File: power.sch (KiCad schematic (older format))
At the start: 24 parts, among them U10 LM1117-3.3, U16 R-78E5.0-1.0, U3 STMPS2151, U7 LM1117-3.3

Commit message: added package field
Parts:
- C1, C15, C2, C20, C32, C36, C9, L1, L2, R5, R6: Package (none) -> 0603
- C14, C47: Package (none) -> Panasonic D
- C25, C41, C5: Package (none) -> Panasonic C
- D1: Package (none) -> SOT-23
- D3, D4: Package (none) -> SOD-123
- U10, U7: Package (none) -> SOT-223
- U3: Package (none) -> SOT-23-5
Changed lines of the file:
@@
 F 4 "Diodes Inc." H 1650 2800 50  0001 C CNN "MFN"
 F 5 "1N5819HW-7-F" H 1650 2800 50  0001 C CNN "MFP"
+F 6 "SOD-123" H 1650 2800 50  0001 C CNN "Package"
 	1    1650 2600
 	1    0    0    -1
@@
 F 4 "Diodes Inc." H 1650 3200 50  0001 C CNN "MFN"
 F 5 "1N5819HW-7-F" H 1650 3200 50  0001 C CNN "MFP"
+F 6 "SOD-123" H 1650 3200 50  0001 C CNN "Package"
 	1    1650 3000
 	-1   0    0    1
@@
 F 4 "Panasonic" H 3800 2550 60  0001 C CNN "MFN"
 F 5 "EEE-FK1V470P" H 3800 2550 60  0001 C CNN "MFP"
+F 6 "Panasonic D" H 3825 2750 50  0001 C CNN "Package"
 	1    3800 2550
 	1    0    0    -1
@@
 F 4 "Texas Instruments" H 5500 3700 60  0001 C CNN "MFN"
 F 5 "LM1117MP-3.3/NOPB" H 5500 3700 60  0001 C CNN "MFP"
+F 6 "SOT-223" H 5350 3925 50  0001 C CNN "Package"
 	1    5500 3700
 	1    0    0    -1
@@
 F 4 "Laird" H 4750 3700 60  0001 C CNN "MFN"
 F 5 "MI0603K300R-10" H 4750 3700 60  0001 C CNN "MFP"
+F 6 "0603" H 4600 3825 50  0001 C CNN "Package"
 	1    4750 3700
 	0    1    1    0
@@
 F 4 "Panasonic" H 6000 3950 60  0001 C CNN "MFN"
 F 5 "EEE-FP1E220AR" H 6000 3950 60  0001 C CNN "MFP"
+F 6 "Panasonic C" H 6025 4150 50  0001 C CNN "Package"
 	1    6000 3950
 	1    0    0    -1
@@
 F 4 "Murata" H 6325 4150 50  0001 C CNN "MFN"
 F 5 "GRM188R71E104JA01J" H 6325 4150 50  0001 C CNN "MFP"
+F 6 "0603" H 6325 4150 50  0001 C CNN "Package"
 	1    6300 3950
 	1    0    0    -1
@@
 F 4 "Texas Instruments" H 5500 4800 60  0001 C CNN "MFN"
 F 5 "LM1117MP-3.3/NOPB" H 5500 4800 60  0001 C CNN "MFP"
+F 6 "SOT-223" H 5350 5025 50  0001 C CNN "Package"
 	1    5500 4800
 	1    0    0    -1
@@
 F 4 "Murata" H 6325 5250 50  0001 C CNN "MFN"
 F 5 "GRM188R71E104JA01J" H 6325 5250 50  0001 C CNN "MFP"
+F 6 "0603" H 6325 5250 50  0001 C CNN "Package"
 	1    6300 5050
 	1    0    0    -1
@@
 F 4 "Murata" H 6225 2850 50  0001 C CNN "MFN"
 F 5 "GRM188R71E104JA01J" H 6225 2850 50  0001 C CNN "MFP"
+F 6 "0603" H 6225 2850 50  0001 C CNN "Package"
 	1    6200 2650
 	1    0    0    -1
@@
 F 4 "Texas Instruments" H 7900 3050 60  0001 C CNN "MFN"
 F 5 "LM4040CIM3-10.0/NOPB" H 7900 3050 60  0001 C CNN "MFP"
+F 6 "SOT-23" H 7900 3250 50  0001 C CNN "Package"
 	1    7900 3050
 	0    -1   -1   0
@@
 F 4 "Panasonic" H 7980 2650 50  0001 C CNN "MFN"
 F 5 "ERJ-3EKF1001V" H 7980 2650 50  0001 C CNN "MFP"
+F 6 "0603" H 7980 2650 50  0001 C CNN "Package"
 	1    7900 2550
 	1    0    0    -1
@@
 F 4 "Murata" H 8225 3250 50  0001 C CNN "MFN"
 F 5 "GRM188R71E104JA01J" H 8225 3250 50  0001 C CNN "MFP"
+F 6 "0603" H 8225 3250 50  0001 C CNN "Package"
 	1    8200 3050
 	1    0    0    -1
@@
 F 4 "STMicroelectronics" H 8900 4200 60  0001 C CNN "MFN"
 F 5 "STMPS2151STR" H 8900 4200 60  0001 C CNN "MFP"
+F 6 "SOT-23-5" H 8900 4500 50  0001 C CNN "Package"
 	1    8900 4200
 	1    0    0    -1
@@
 F 4 "Panasonic" H 8280 4550 50  0001 C CNN "MFN"
 F 5 "ERJ-3EKF1002V" H 8280 4550 50  0001 C CNN "MFP"
+F 6 "0603" H 8280 4550 50  0001 C CNN "Package"
 	1    8200 4450
 	1    0    0    -1
@@
 F 4 "Panasonic" H 3800 3050 60  0001 C CNN "MFN"
 F 5 "EEE-FK1V470P" H 3800 3050 60  0001 C CNN "MFP"
+F 6 "Panasonic D" H 3825 3250 50  0001 C CNN "Package"
 	1    3800 3050
 	1    0    0    -1
@@
 F 4 "Panasonic" H 6000 5050 60  0001 C CNN "MFN"
 F 5 "EEE-FP1E220AR" H 6000 5050 60  0001 C CNN "MFP"
+F 6 "Panasonic C" H 6025 5250 50  0001 C CNN "Package"
 	1    6000 5050
 	1    0    0    -1
@@
 F 4 "Panasonic" H 5900 2650 60  0001 C CNN "MFN"
 F 5 "EEE-FP1E220AR" H 5900 2650 60  0001 C CNN "MFP"
+F 6 "Panasonic C" H 5925 2850 50  0001 C CNN "Package"
 	1    5900 2650
 	1    0    0    -1
@@
 F 4 "Laird" H 4750 4800 60  0001 C CNN "MFN"
 F 5 "MI0603K300R-10" H 4750 4800 60  0001 C CNN "MFP"
+F 6 "0603" H 4600 4925 50  0001 C CNN "Package"
 	1    4750 4800
 	0    1    1    0
@@
 F 4 "Murata" H 5000 3950 60  0001 C CNN "MFN"
 F 5 "GRM188R71E104JA01J" H 5000 3950 60  0001 C CNN "MFP"
+F 6 "0603" H 5025 4150 50  0001 C CNN "Package"
 	1    5000 3950
 	1    0    0    -1
@@
 F 4 "Murata" H 5000 5050 60  0001 C CNN "MFN"
 F 5 "GRM188R71E104JA01J" H 5000 5050 60  0001 C CNN "MFP"
+F 6 "0603" H 5025 5250 50  0001 C CNN "Package"
 	1    5000 5050
 	1    0    0    -1
@@
 F 4 "Murata" H 4800 2650 60  0001 C CNN "MFN"
 F 5 "GRM188R71E104JA01J" H 4800 2650 60  0001 C CNN "MFP"
+F 6 "0603" H 4825 2850 50  0001 C CNN "Package"
 	1    4800 2650
 	1    0    0    -1

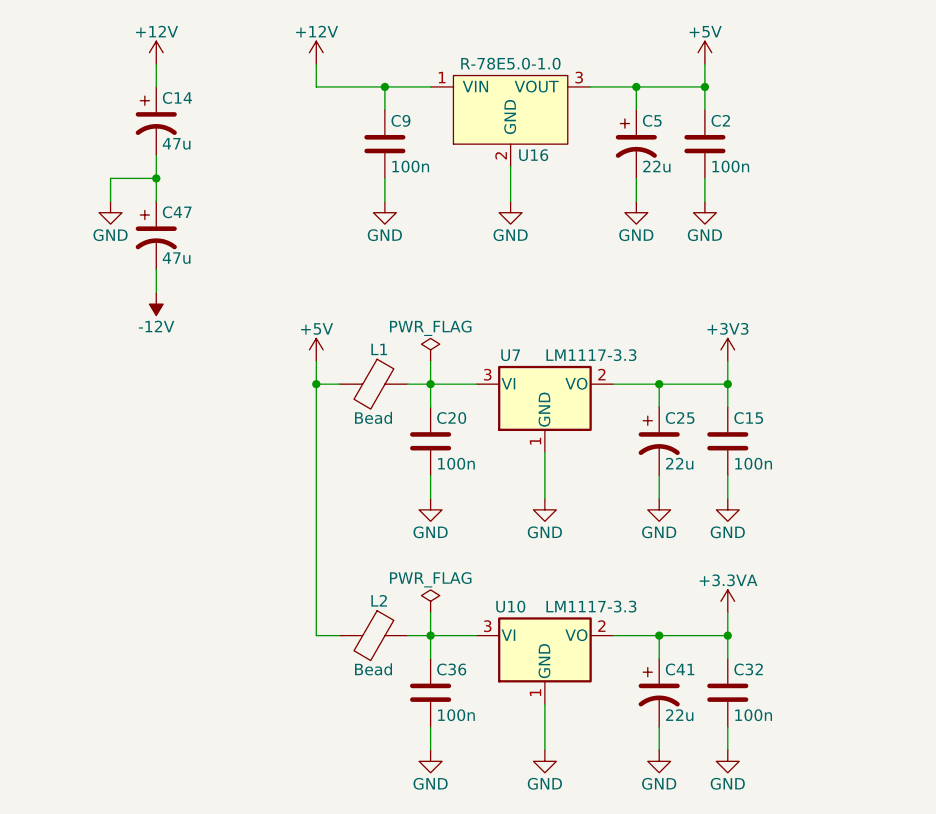
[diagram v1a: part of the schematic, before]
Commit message: renumbered components
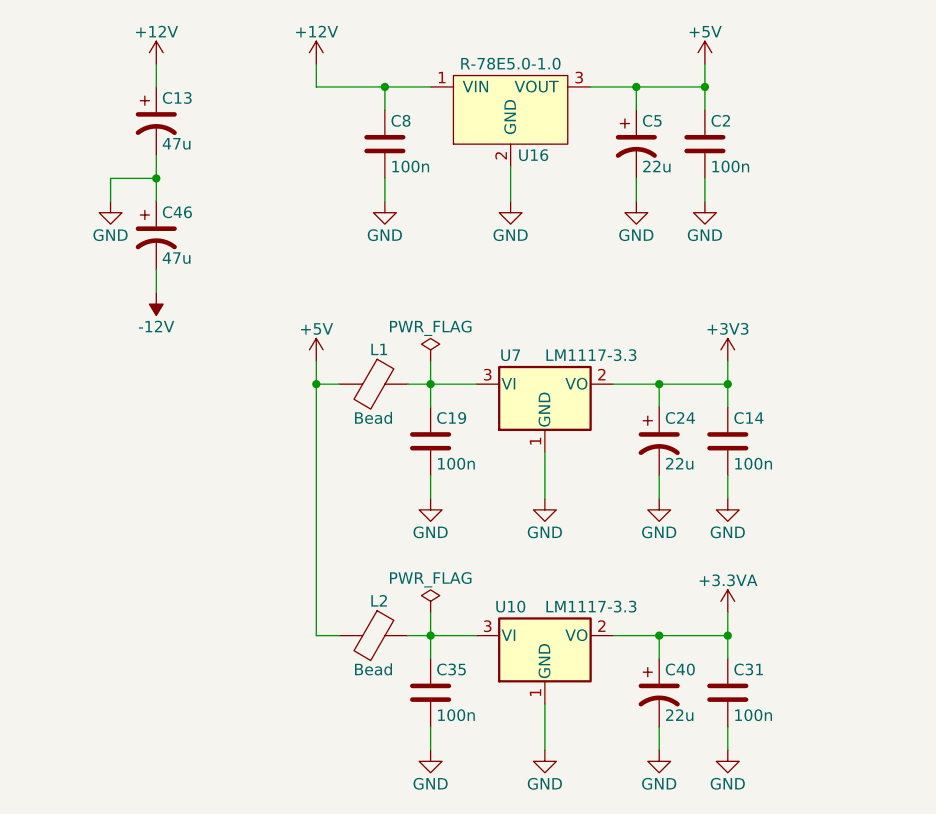
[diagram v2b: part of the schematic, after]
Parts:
- renumbered C14 to C13, C15 to C14, C20 to C19, C25 to C24, C32 to C31, C36 to C35, C41 to C40, C47 to C46, C9 to C8
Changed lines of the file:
@@
 $EndComp
 $Comp
-L CP1 C14
+L CP1 C13
 U 1 1 59ADD50C
 P 3800 2550
-F 0 "C14" H 3825 2650 50  0000 L CNN
+F 0 "C13" H 3825 2650 50  0000 L CNN
 F 1 "47u" H 3825 2450 50  0000 L CNN
 F 2 "Capacitors_SMD:CP_Elec_6.3x5.7" H 3800 2550 50  0001 C CNN
@@
 $EndComp
 $Comp
-L CP1 C25
+L CP1 C24
 U 1 1 59DEC56E
 P 6000 3950
-F 0 "C25" H 6025 4050 50  0000 L CNN
+F 0 "C24" H 6025 4050 50  0000 L CNN
 F 1 "22u" H 6025 3850 50  0000 L CNN
 F 2 "Capacitors_SMD:CP_Elec_5x5.8" H 6000 3950 50  0001 C CNN
@@
 $EndComp
 $Comp
-L C C15
+L C C14
 U 1 1 59DEC574
 P 6300 3950
-F 0 "C15" H 6325 4050 50  0000 L CNN
+F 0 "C14" H 6325 4050 50  0000 L CNN
 F 1 "100n" H 6325 3850 50  0000 L CNN
 F 2 "w_capacitor:C_0603" H 6338 3800 50  0001 C CNN
@@
 $EndComp
 $Comp
-L C C32
+L C C31
 U 1 1 59DEC80C
 P 6300 5050
-F 0 "C32" H 6325 5150 50  0000 L CNN
+F 0 "C31" H 6325 5150 50  0000 L CNN
 F 1 "100n" H 6325 4950 50  0000 L CNN
 F 2 "w_capacitor:C_0603" H 6338 4900 50  0001 C CNN
@@
 $EndComp
 $Comp
-L CP1 C47
+L CP1 C46
 U 1 1 59E0E120
 P 3800 3050
-F 0 "C47" H 3825 3150 50  0000 L CNN
+F 0 "C46" H 3825 3150 50  0000 L CNN
 F 1 "47u" H 3825 2950 50  0000 L CNN
 F 2 "Capacitors_SMD:CP_Elec_6.3x5.7" H 3800 3050 50  0001 C CNN
@@
 $EndComp
 $Comp
-L CP1 C41
+L CP1 C40
 U 1 1 59E0FE4F
 P 6000 5050
-F 0 "C41" H 6025 5150 50  0000 L CNN
+F 0 "C40" H 6025 5150 50  0000 L CNN
 F 1 "22u" H 6025 4950 50  0000 L CNN
 F 2 "Capacitors_SMD:CP_Elec_5x5.8" H 6000 5050 50  0001 C CNN
@@
 $EndComp
 $Comp
-L C C20
+L C C19
 U 1 1 59E52EDD
 P 5000 3950
-F 0 "C20" H 5025 4050 50  0000 L CNN
+F 0 "C19" H 5025 4050 50  0000 L CNN
 F 1 "100n" H 5025 3850 50  0000 L CNN
 F 2 "w_capacitor:C_0603" H 5038 3800 50  0001 C CNN
@@
 $EndComp
 $Comp
-L C C36
+L C C35
 U 1 1 59E53513
 P 5000 5050
-F 0 "C36" H 5025 5150 50  0000 L CNN
+F 0 "C35" H 5025 5150 50  0000 L CNN
 F 1 "100n" H 5025 4950 50  0000 L CNN
 F 2 "w_capacitor:C_0603" H 5038 4900 50  0001 C CNN
@@
 $EndComp
 $Comp
-L C C9
+L C C8
 U 1 1 59E535E8
 P 4800 2650
-F 0 "C9" H 4825 2750 50  0000 L CNN
+F 0 "C8" H 4825 2750 50  0000 L CNN
 F 1 "100n" H 4825 2550 50  0000 L CNN
 F 2 "w_capacitor:C_0603" H 4838 2500 50  0001 C CNN

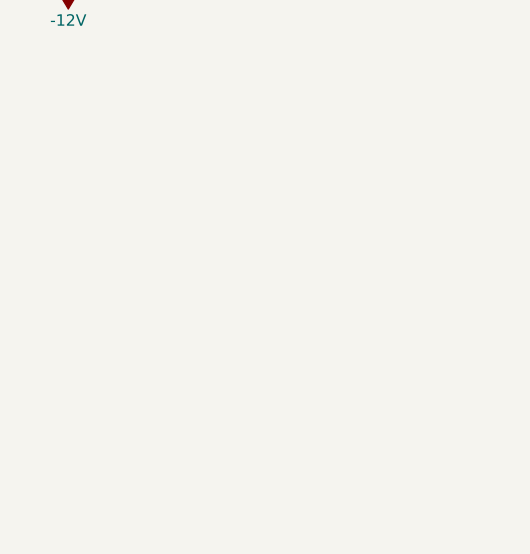
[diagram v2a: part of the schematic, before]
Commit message: cleanup schematics and updated to revision 0.3
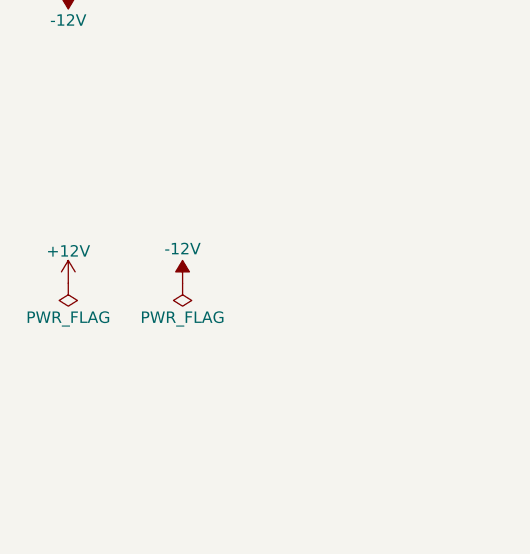
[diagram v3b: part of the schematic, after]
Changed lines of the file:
@@
 Sheet 3 8
 Title "per|former eurorack sequencer"
-Date ""
-Rev "0.2"
+Date "2018-08-26"
+Rev "0.3"
 Comp "westlicht"
 Comment1 "cc-by-sa"
@@
 $EndDescr
 $Comp
-L +12V #PWR025
+L +12V #PWR5
 U 1 1 59ADCE23
 P 1400 2500
-F 0 "#PWR025" H 1400 2350 50  0001 C CNN
+F 0 "#PWR5" H 1400 2350 50  0001 C CNN
 F 1 "+12V" H 1400 2640 50  0000 C CNN
 F 2 "" H 1400 2500 50  0001 C CNN
@@
 $EndComp
 $Comp
-L -12V #PWR212
+L -12V #PWR12
 U 1 1 59ADCE37
 P 1400 3100
-F 0 "#PWR212" H 1400 3200 50  0001 C CNN
+F 0 "#PWR12" H 1400 3200 50  0001 C CNN
 F 1 "-12V" H 1400 3250 50  0000 C CNN
 F 2 "" H 1400 3100 50  0001 C CNN
@@
 $EndComp
 $Comp
-L GND #PWR026
+L GND #PWR6
 U 1 1 59ADD2AE
 P 2800 2900
-F 0 "#PWR026" H 2800 2650 50  0001 C CNN
+F 0 "#PWR6" H 2800 2650 50  0001 C CNN
 F 1 "GND" H 2800 2750 50  0000 C CNN
 F 2 "" H 2800 2900 50  0001 C CNN
@@
 $EndComp
 $Comp
-L -12V #PWR213
+L -12V #PWR13
 U 1 1 59ADD571
 P 3800 3300
-F 0 "#PWR213" H 3800 3400 50  0001 C CNN
+F 0 "#PWR13" H 3800 3400 50  0001 C CNN
 F 1 "-12V" H 3800 3450 50  0000 C CNN
 F 2 "" H 3800 3300 50  0001 C CNN
@@
 $EndComp
 $Comp
-L +12V #PWR027
+L +12V #PWR1
 U 1 1 59ADD597
 P 3800 2300
-F 0 "#PWR027" H 3800 2150 50  0001 C CNN
+F 0 "#PWR1" H 3800 2150 50  0001 C CNN
 F 1 "+12V" H 3800 2440 50  0000 C CNN
 F 2 "" H 3800 2300 50  0001 C CNN
@@
 $EndComp
 $Comp
-L GND #PWR028
+L GND #PWR7
 U 1 1 59ADD670
 P 3600 2900
-F 0 "#PWR028" H 3600 2650 50  0001 C CNN
+F 0 "#PWR7" H 3600 2650 50  0001 C CNN
 F 1 "GND" H 3600 2750 50  0000 C CNN
 F 2 "" H 3600 2900 50  0001 C CNN
@@
 $EndComp
 $Comp
-L GND #PWR029
+L GND #PWR18
 U 1 1 59DEC57A
 P 5000 4200
-F 0 "#PWR029" H 5000 3950 50  0001 C CNN
+F 0 "#PWR18" H 5000 3950 50  0001 C CNN
 F 1 "GND" H 5000 4050 50  0000 C CNN
 F 2 "" H 5000 4200 50  0001 C CNN
@@
 $EndComp
 $Comp
-L GND #PWR030
+L GND #PWR20
 U 1 1 59DEC580
 P 6000 4200
-F 0 "#PWR030" H 6000 3950 50  0001 C CNN
+F 0 "#PWR20" H 6000 3950 50  0001 C CNN
 F 1 "GND" H 6000 4050 50  0000 C CNN
 F 2 "" H 6000 4200 50  0001 C CNN
@@
 $EndComp
 $Comp
-L GND #PWR031
+L GND #PWR21
 U 1 1 59DEC586
 P 6300 4200
-F 0 "#PWR031" H 6300 3950 50  0001 C CNN
+F 0 "#PWR21" H 6300 3950 50  0001 C CNN
 F 1 "GND" H 6300 4050 50  0000 C CNN
 F 2 "" H 6300 4200 50  0001 C CNN
@@
 $EndComp
 $Comp
-L +3V3 #PWR032
+L +3V3 #PWR16
 U 1 1 59DEC592
 P 6300 3600
-F 0 "#PWR032" H 6300 3450 50  0001 C CNN
+F 0 "#PWR16" H 6300 3450 50  0001 C CNN
 F 1 "+3V3" H 6300 3740 50  0000 C CNN
 F 2 "" H 6300 3600 50  0001 C CNN
@@
 $EndComp
 $Comp
-L GND #PWR033
+L GND #PWR19
 U 1 1 59DEC598
 P 5500 4200
-F 0 "#PWR033" H 5500 3950 50  0001 C CNN
+F 0 "#PWR19" H 5500 3950 50  0001 C CNN
 F 1 "GND" H 5500 4050 50  0000 C CNN
 F 2 "" H 5500 4200 50  0001 C CNN
@@
 $EndComp
 $Comp
-L GND #PWR034
+L GND #PWR27
 U 1 1 59DEC812
 P 5000 5300
-F 0 "#PWR034" H 5000 5050 50  0001 C CNN
+F 0 "#PWR27" H 5000 5050 50  0001 C CNN
 F 1 "GND" H 5000 5150 50  0000 C CNN
 F 2 "" H 5000 5300 50  0001 C CNN
@@
 $EndComp
 $Comp
-L GND #PWR035
+L GND #PWR29
 U 1 1 59DEC818
 P 6000 5300
-F 0 "#PWR035" H 6000 5050 50  0001 C CNN
+F 0 "#PWR29" H 6000 5050 50  0001 C CNN
 F 1 "GND" H 6000 5150 50  0000 C CNN
 F 2 "" H 6000 5300 50  0001 C CNN
@@
 $EndComp
 $Comp
-L GND #PWR036
+L GND #PWR30
 U 1 1 59DEC81E
 P 6300 5300
-F 0 "#PWR036" H 6300 5050 50  0001 C CNN
+F 0 "#PWR30" H 6300 5050 50  0001 C CNN
 F 1 "GND" H 6300 5150 50  0000 C CNN
 F 2 "" H 6300 5300 50  0001 C CNN
@@
 $EndComp
 $Comp
-L GND #PWR037
+L GND #PWR28
 U 1 1 59DEC82A
 P 5500 5300
-F 0 "#PWR037" H 5500 5050 50  0001 C CNN
+F 0 "#PWR28" H 5500 5050 50  0001 C CNN
 F 1 "GND" H 5500 5150 50  0000 C CNN
 F 2 "" H 5500 5300 50  0001 C CNN
@@
 $EndComp
 $Comp
-L +12V #PWR038
+L +12V #PWR2
 U 1 1 59DECCAB
 P 4500 2300
-F 0 "#PWR038" H 4500 2150 50  0001 C CNN
+F 0 "#PWR2" H 4500 2150 50  0001 C CNN
 F 1 "+12V" H 4500 2440 50  0000 C CNN
 F 2 "" H 4500 2300 50  0001 C CNN
@@
 $EndComp
 $Comp
-L +3.3VA #PWR039
+L +3.3VA #PWR24
 U 1 1 59DED3E1
 P 6300 4700
-F 0 "#PWR039" H 6300 4550 50  0001 C CNN
+F 0 "#PWR24" H 6300 4550 50  0001 C CNN
 F 1 "+3.3VA" H 6300 4840 50  0000 C CNN
 F 2 "" H 6300 4700 50  0001 C CNN
@@
 $EndComp
 $Comp
-L GND #PWR040
+L GND #PWR8
 U 1 1 59DED9CB
 P 4800 2900
-F 0 "#PWR040" H 4800 2650 50  0001 C CNN
+F 0 "#PWR8" H 4800 2650 50  0001 C CNN
 F 1 "GND" H 4800 2750 50  0000 C CNN
 F 2 "" H 4800 2900 50  0001 C CNN
@@
 $EndComp
 $Comp
-L GND #PWR041
+L GND #PWR10
 U 1 1 59DED9D1
 P 5900 2900
-F 0 "#PWR041" H 5900 2650 50  0001 C CNN
+F 0 "#PWR10" H 5900 2650 50  0001 C CNN
 F 1 "GND" H 5900 2750 50  0000 C CNN
 F 2 "" H 5900 2900 50  0001 C CNN
@@
 $EndComp
 $Comp
-L GND #PWR042
+L GND #PWR11
 U 1 1 59DED9D7
 P 6200 2900
-F 0 "#PWR042" H 6200 2650 50  0001 C CNN
+F 0 "#PWR11" H 6200 2650 50  0001 C CNN
 F 1 "GND" H 6200 2750 50  0000 C CNN
 F 2 "" H 6200 2900 50  0001 C CNN
@@
 $EndComp
 $Comp
-L GND #PWR043
+L GND #PWR9
 U 1 1 59DED9DD
 P 5350 2900
-F 0 "#PWR043" H 5350 2650 50  0001 C CNN
+F 0 "#PWR9" H 5350 2650 50  0001 C CNN
 F 1 "GND" H 5350 2750 50  0000 C CNN
 F 2 "" H 5350 2900 50  0001 C CNN
@@
 $EndComp
 $Comp
-L +5V #PWR044
+L +5V #PWR3
 U 1 1 59DEDB3A
 P 6200 2300
-F 0 "#PWR044" H 6200 2150 50  0001 C CNN
+F 0 "#PWR3" H 6200 2150 50  0001 C CNN
 F 1 "+5V" H 6200 2440 50  0000 C CNN
 F 2 "" H 6200 2300 50  0001 C CNN
@@
 $EndComp
 $Comp
-L -12V #PWR204
+L -12V #PWR4
 U 1 1 59DF1046
 P 7900 2300
-F 0 "#PWR204" H 7900 2400 50  0001 C CNN
+F 0 "#PWR4" H 7900 2400 50  0001 C CNN
 F 1 "-12V" H 7900 2450 50  0000 C CNN
 F 2 "" H 7900 2300 50  0001 C CNN
@@
 $EndComp
 $Comp
-L GND #PWR045
+L GND #PWR14
 U 1 1 59DF1FC9
 P 7900 3400
-F 0 "#PWR045" H 7900 3150 50  0001 C CNN
+F 0 "#PWR14" H 7900 3150 50  0001 C CNN
 F 1 "GND" H 7900 3250 50  0000 C CNN
 F 2 "" H 7900 3400 50  0001 C CNN
@@
 $EndComp
 $Comp
-L +5V #PWR046
+L +5V #PWR17
 U 1 1 59DFDC6E
 P 8400 4000
-F 0 "#PWR046" H 8400 3850 50  0001 C CNN
+F 0 "#PWR17" H 8400 3850 50  0001 C CNN
 F 1 "+5V" H 8400 4140 50  0000 C CNN
 F 2 "" H 8400 4000 50  0001 C CNN
@@
 $EndComp
 $Comp
-L GND #PWR047
+L GND #PWR26
 U 1 1 59DFDCE5
 P 8400 4700
-F 0 "#PWR047" H 8400 4450 50  0001 C CNN
+F 0 "#PWR26" H 8400 4450 50  0001 C CNN
 F 1 "GND" H 8400 4550 50  0000 C CNN
 F 2 "" H 8400 4700 50  0001 C CNN
@@
 $EndComp
 $Comp
-L GND #PWR048
+L GND #PWR25
 U 1 1 59E00E5E
 P 8200 4700
-F 0 "#PWR048" H 8200 4450 50  0001 C CNN
+F 0 "#PWR25" H 8200 4450 50  0001 C CNN
 F 1 "GND" H 8200 4550 50  0000 C CNN
 F 2 "" H 8200 4700 50  0001 C CNN
@@
 $EndComp
 $Comp
-L PWR_FLAG #FLG049
+L PWR_FLAG #FLG1
 U 1 1 59F34CFD
 P 5000 3600
-F 0 "#FLG049" H 5000 3675 50  0001 C CNN
+F 0 "#FLG1" H 5000 3675 50  0001 C CNN
 F 1 "PWR_FLAG" H 5000 3750 50  0000 C CNN
 F 2 "" H 5000 3600 50  0001 C CNN
@@
 $EndComp
 $Comp
-L PWR_FLAG #FLG050
+L PWR_FLAG #FLG4
 U 1 1 59F34D75
 P 5000 4700
-F 0 "#FLG050" H 5000 4775 50  0001 C CNN
+F 0 "#FLG4" H 5000 4775 50  0001 C CNN
 F 1 "PWR_FLAG" H 5000 4850 50  0000 C CNN
 F 2 "" H 5000 4700 50  0001 C CNN
@@
 $EndComp
 $Comp
-L +5V #PWR051
+L +5V #PWR15
 U 1 1 5AEF8A3B
 P 4500 3600
-F 0 "#PWR051" H 4500 3450 50  0001 C CNN
+F 0 "#PWR15" H 4500 3450 50  0001 C CNN
 F 1 "+5V" H 4500 3740 50  0000 C CNN
 F 2 "" H 4500 3600 50  0001 C CNN
@@
 Connection ~ 8200 4200
 Connection ~ 7900 2800
+$Comp
+L +12V #PWR22
+U 1 1 5B8366B1
+P 1400 4400
+F 0 "#PWR22" H 1400 4250 50  0001 C CNN
+F 1 "+12V" H 1400 4540 50  0000 C CNN
+F 2 "" H 1400 4400 50  0001 C CNN
+F 3 "" H 1400 4400 50  0001 C CNN
+	1    1400 4400
+	1    0    0    -1
+$EndComp
+$Comp
+L -12V #PWR23
+U 1 1 5B83670D
+P 1900 4400
+F 0 "#PWR23" H 1900 4500 50  0001 C CNN
+F 1 "-12V" H 1900 4550 50  0000 C CNN
+F 2 "" H 1900 4400 50  0001 C CNN
+F 3 "" H 1900 4400 50  0001 C CNN
+	1    1900 4400
+	1    0    0    -1
+$EndComp
+$Comp
+L PWR_FLAG #FLG2
+U 1 1 5B836769
+P 1400 4400
+F 0 "#FLG2" H 1400 4475 50  0001 C CNN
+F 1 "PWR_FLAG" H 1400 4550 50  0000 C CNN
+F 2 "" H 1400 4400 50  0001 C CNN
+F 3 "" H 1400 4400 50  0001 C CNN
+	1    1400 4400
+	-1   0    0    1
+$EndComp
+$Comp
+L PWR_FLAG #FLG3
+U 1 1 5B836855
+P 1900 4400
+F 0 "#FLG3" H 1900 4475 50  0001 C CNN
+F 1 "PWR_FLAG" H 1900 4550 50  0000 C CNN
+F 2 "" H 1900 4400 50  0001 C CNN
+F 3 "" H 1900 4400 50  0001 C CNN
+	1    1900 4400
+	-1   0    0    1
+$EndComp
 $EndSCHEMATC

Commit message: cleaned up schematics
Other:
- note added: "-10V REFERENCE"
- note added: "3.3V SUPPLY (ANALOG)"
- note added: "3.3V SUPPLY (DIGITAL)"
- note added: "5V 1A DC-DC step down converter"
- note added: "5V SUPPLY"
- note added: "5V SUPPLY (USB)"
- note added: "POWER INLET"
- note added: "Reverse protection and filtering for +12V/-12V rails"
- moved on the sheet: C1, C13, C14, C19, C2, C24, C31, C35, C40, C46, C5, C8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

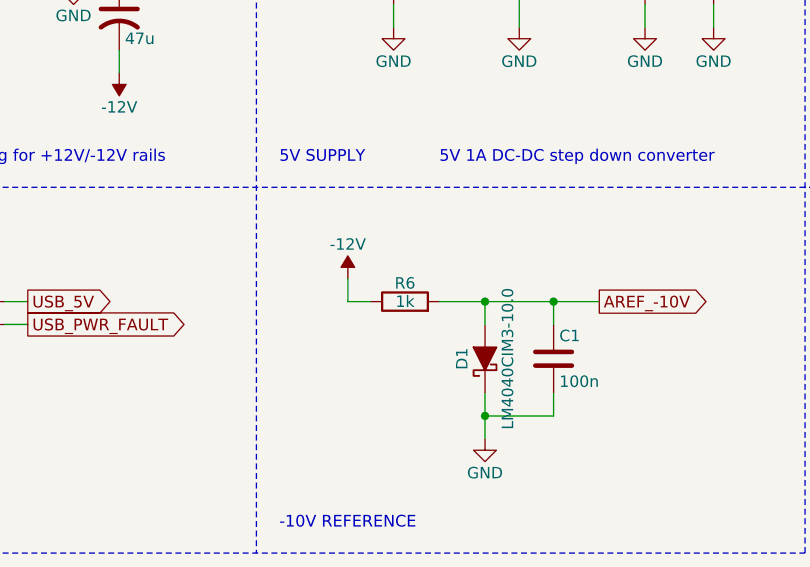
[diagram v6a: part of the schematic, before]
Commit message: renumbered components
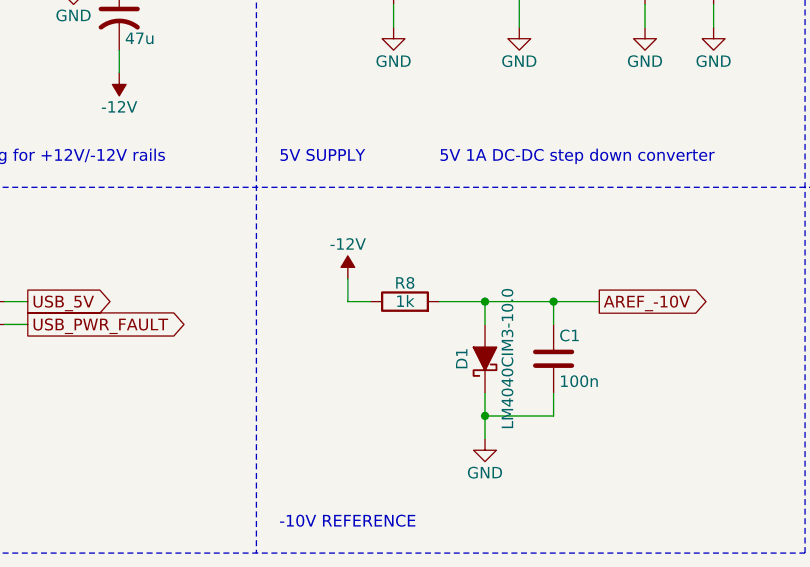
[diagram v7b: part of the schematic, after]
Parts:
- renumbered R6 to R8
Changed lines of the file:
@@
 $EndComp
 $Comp
-L R R6
+L R R8
 U 1 1 59DF10B1
 P 4250 3000
-F 0 "R6" V 4330 3000 50  0000 C CNN
+F 0 "R8" V 4330 3000 50  0000 C CNN
 F 1 "1k" V 4250 3000 50  0000 C CNN
 F 2 "w_resistor:R_0603" V 4180 3000 50  0001 C CNN
